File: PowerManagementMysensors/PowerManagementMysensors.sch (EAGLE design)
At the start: 57 parts, among them IC2 AT25DF512C-SSHN-B, U2 SI2399DS-T1-GE3, U3 SI2399DS-T1-GE3, U4 MCP1640BT-I/CHY, U5 TPS61222DCKT, U6 BSS123-7-F, U7 SI2399DS-T1-GE3

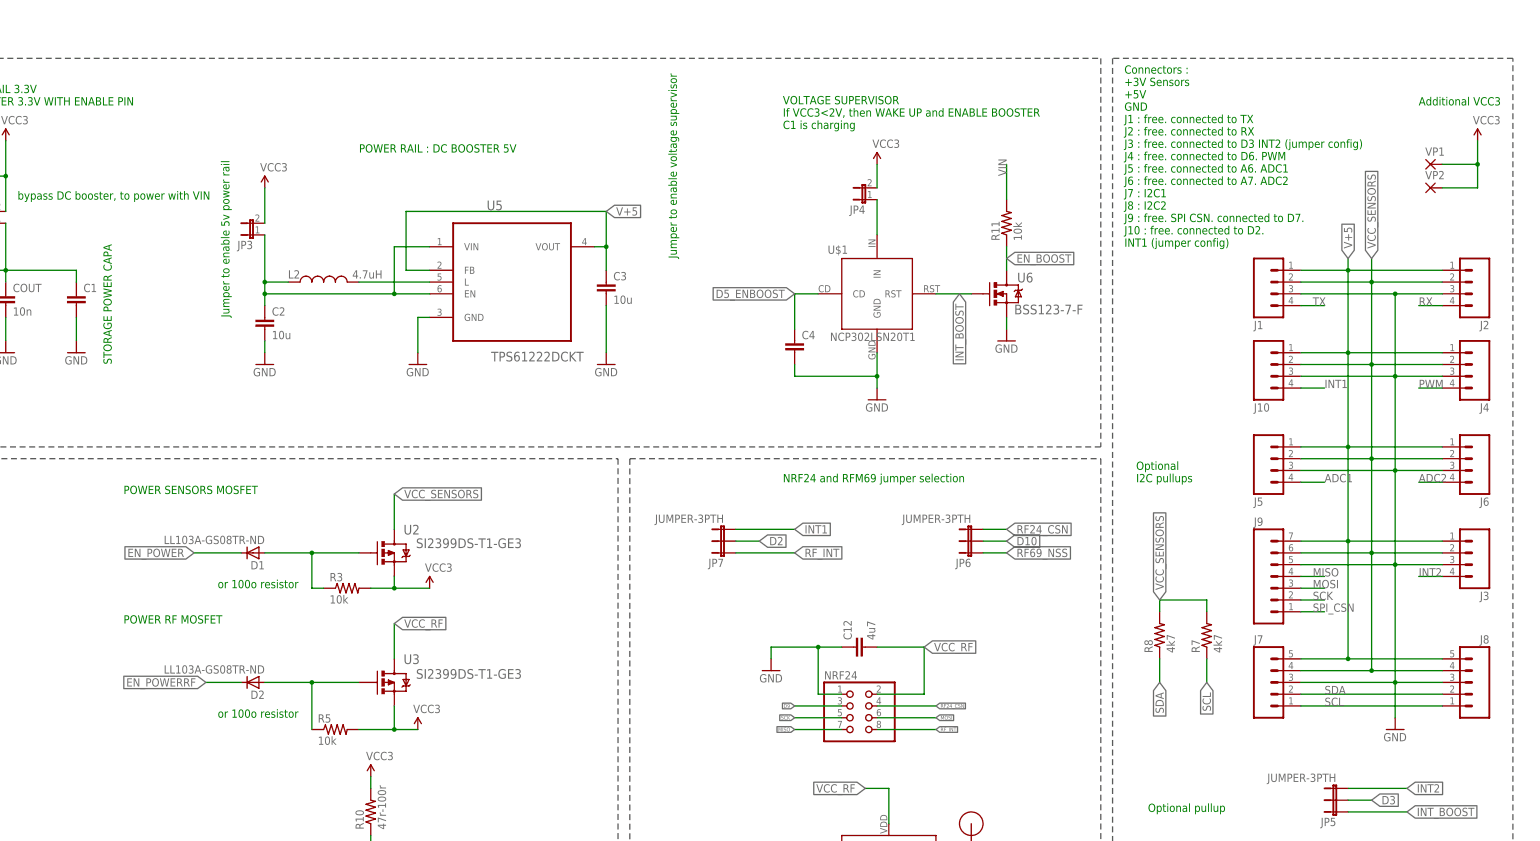
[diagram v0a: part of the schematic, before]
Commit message: many changes
removed external TX and RX
External I2C3 added
Reverse polarity added
Optional pull up for D6 added
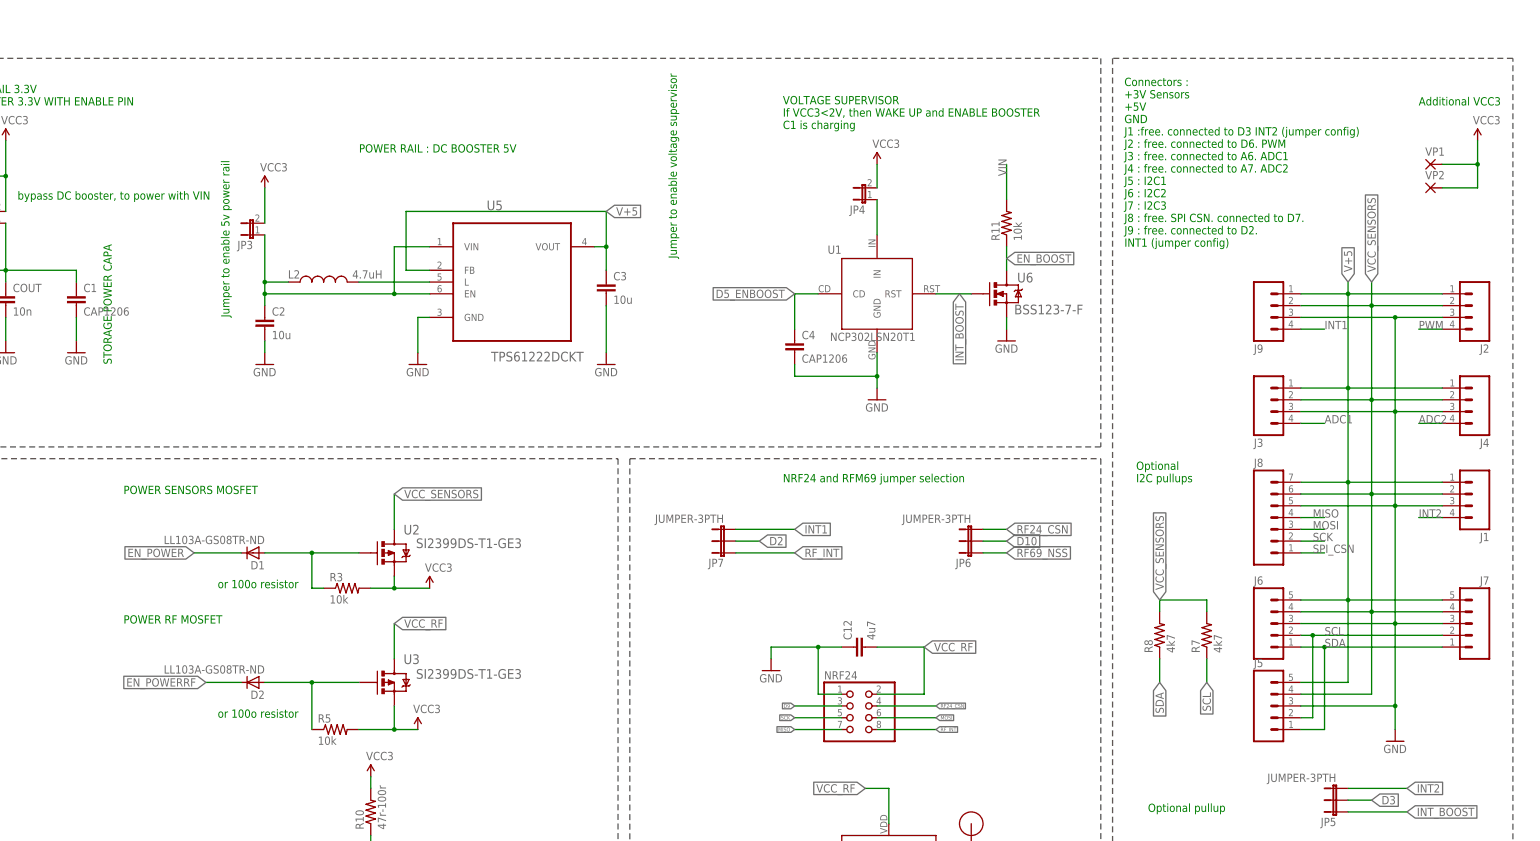
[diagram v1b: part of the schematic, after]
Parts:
- removed J10: (no value), SparkFun-Connectors:M041X04_NO_SILK
- C1, C4: value (none) -> CAP1206
- C12: device SparkFun-Capacitors:CAP1206 -> SparkFun-Passives:CAP1206
- J5, J6: device SparkFun-Connectors:M041X04_NO_SILK -> SparkFun-Connectors:M05NO_SILK
- J8: device SparkFun-Connectors:M05NO_SILK -> SparkFun-Connectors:M07
- J9: device SparkFun-Connectors:M07 -> SparkFun-Connectors:M041X04_NO_SILK
- renumbered U$1 to U1
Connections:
- net ADC1: now also J3.4; no longer J5.4
- net ADC2: now also J4.4; no longer J6.4
- net GND: now also J8.5, J9.3; no longer J10.3, J8.3, J9.5
- net INT1: now also J9.4; no longer J10.4
- net INT2: now also J1.4; no longer J3.4
- net MISO: now also J8.4; no longer J9.4
- net MOSI: now also J8.3; no longer J9.3
- net PWM: now also J2.4; no longer J4.4
- net RX: no longer J2.4
- net SCK: now also J8.2; no longer J9.2
- net SCL: now also J5.2, J6.2, J7.2; no longer J7.1, J8.1
- net SDA: now also J5.1, J6.1, J7.1; no longer J7.2, J8.2
- net SPI_CSN: now also J8.1; no longer J9.1
- net TX: no longer J1.4
- net V+5: now also J5.5, J6.5, J8.7, J9.1; no longer J10.1, J5.1, J6.1, J8.5, J9.7
- net VCC_SENSORS: now also J5.4, J6.4, J8.6, J9.2; no longer J10.2, J5.2, J6.2, J8.4, J9.6
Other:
- note added: "Connectors : +3V Sensors +5V GND J1 :free. connected to D3 INT2 (jumper config) J2 : free. connected to D6. PWM J3 : free. connected to A6. ADC1 J4 : free. connected to A7. ADC2 J5 : I2C1 J6 : I2C2 J7 : I2C3 J8 : free. SPI CSN. connected to D7. J9 : free. connected to D2. INT1 (jumper config)"
- note removed: "Connectors : +3V Sensors +5V GND J1 : free. connected to TX J2 : free. connected to RX J3 : free. connected to D3 INT2 (jumper config) J4 : free. connected to D6. PWM J5 : free. connected to A6. ADC1 J6 : free. connected to A7. ADC2 J7 : I2C1 J8 : I2C2 J9 : free. SPI CSN. connected to D7. J10 : free. connected to D2. INT1 (jumper config)"
- moved on the sheet: J1, J2, J3, J4, J7

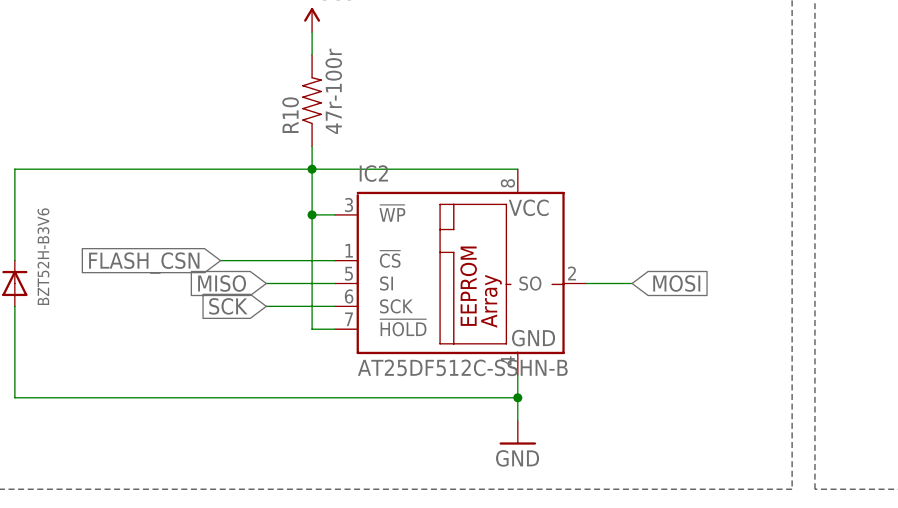
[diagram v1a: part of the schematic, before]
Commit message: rerouting eeprom for ota
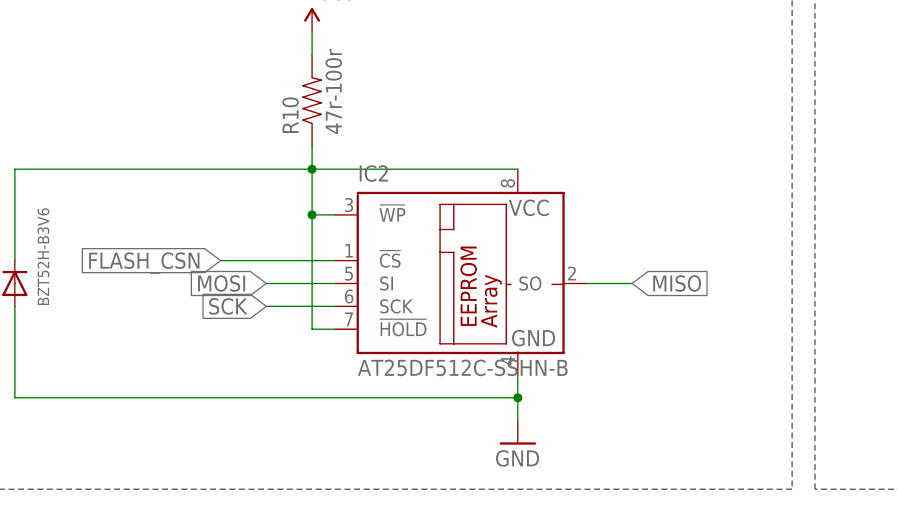
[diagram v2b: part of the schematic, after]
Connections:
- net MISO: now also IC2.SO; no longer IC2.SI
- net MOSI: now also IC2.SI; no longer IC2.SO
